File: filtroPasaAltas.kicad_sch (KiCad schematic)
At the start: 7 parts, among them U2 TL082

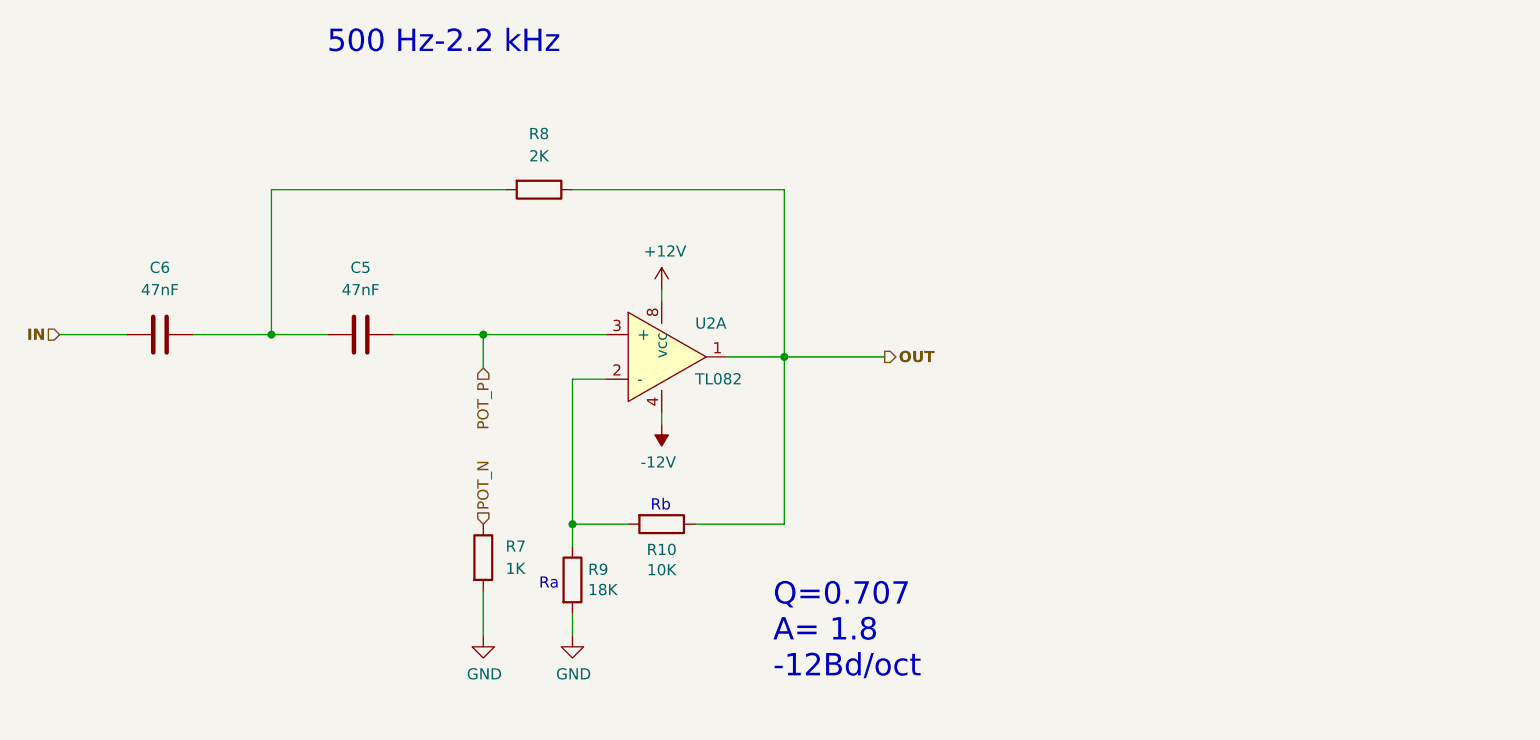
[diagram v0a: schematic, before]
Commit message: agregando control de volumen de medios, corrigiendo espacio de potenciometro doble
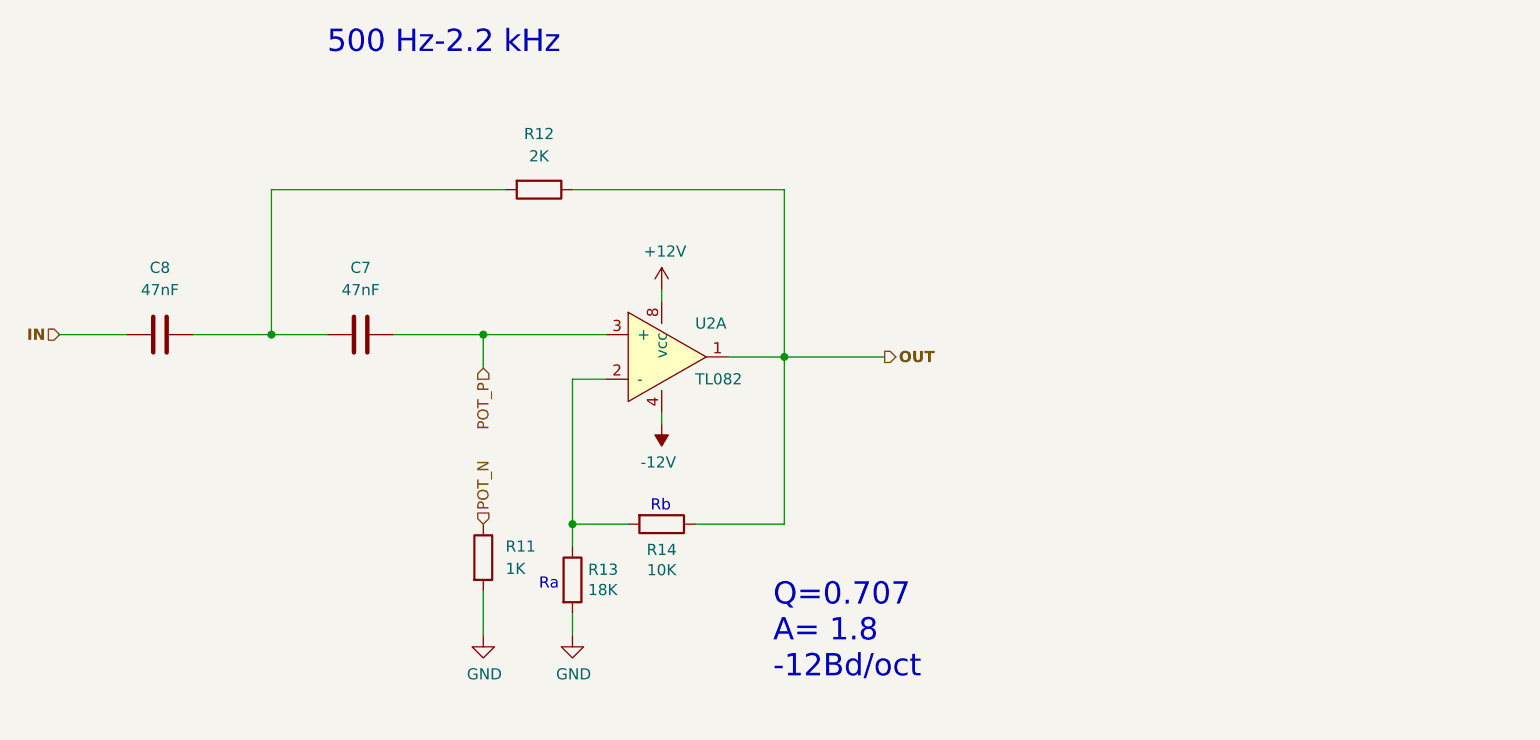
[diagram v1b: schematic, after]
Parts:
- renumbered C5 to C7, C6 to C8, R7 to R11, R8 to R12, R9 to R13, R10 to R14
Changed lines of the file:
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@@
   (symbol (lib_id "Device:R") (at 86.36 88.9 0)
     (in_bom yes) (on_board yes) (fields_autoplaced)
-    (property "Reference" "R7" (id 0) (at 88.9 87.6299 0)
+    (property "Reference" "R11" (id 0) (at 88.9 87.6299 0)
       (effects (font (size 1.27 1.27)) (justify left))
     )
@@
   (symbol (lib_id "Device:R") (at 92.71 46.99 270)
     (in_bom yes) (on_board yes) (fields_autoplaced)
-    (property "Reference" "R8" (id 0) (at 92.71 40.64 90))
+    (property "Reference" "R12" (id 0) (at 92.71 40.64 90))
     (property "Value" "2K" (id 1) (at 92.71 43.18 90))
     (property "Footprint" "Resistor_THT:R_Axial_DIN0207_L6.3mm_D2.5mm_P10.16mm_Horizontal" (id 2) (at 92.71 45.212 90)
@@
   (symbol (lib_id "Device:R") (at 96.52 91.44 0)
     (in_bom yes) (on_board yes)
-    (property "Reference" "R9" (id 0) (at 98.298 90.2716 0)
+    (property "Reference" "R13" (id 0) (at 98.298 90.2716 0)
       (effects (font (size 1.27 1.27)) (justify left))
     )
@@
   (symbol (lib_id "Device:R") (at 106.68 85.09 270)
     (in_bom yes) (on_board yes)
-    (property "Reference" "R10" (id 0) (at 106.68 88.011 90))
+    (property "Reference" "R14" (id 0) (at 106.68 88.011 90))
     (property "Value" "10K" (id 1) (at 106.68 90.3224 90))
     (property "Footprint" "Resistor_THT:R_Axial_DIN0207_L6.3mm_D2.5mm_P10.16mm_Horizontal" (id 2) (at 106.68 83.312 90)
@@
   (symbol (lib_id "Device:C") (at 49.53 63.5 270)
     (in_bom yes) (on_board yes) (fields_autoplaced)
-    (property "Reference" "C6" (id 0) (at 49.53 55.88 90))
+    (property "Reference" "C8" (id 0) (at 49.53 55.88 90))
     (property "Value" "47nF" (id 1) (at 49.53 58.42 90))
     (property "Footprint" "Capacitor_THT:C_Disc_D4.3mm_W1.9mm_P5.00mm" (id 2) (at 45.72 64.4652 0)
@@
   (symbol (lib_id "Device:C") (at 72.39 63.5 270)
     (in_bom yes) (on_board yes) (fields_autoplaced)
-    (property "Reference" "C5" (id 0) (at 72.39 55.88 90))
+    (property "Reference" "C7" (id 0) (at 72.39 55.88 90))
     (property "Value" "47nF" (id 1) (at 72.39 58.42 90))
     (property "Footprint" "Capacitor_THT:C_Disc_D4.3mm_W1.9mm_P5.00mm" (id 2) (at 68.58 64.4652 0)
@@
     (pin "4")
     (pin "8")
-    (pin "1")
-    (pin "2")
-    (pin "3")
+    (pin "5")
+    (pin "6")
+    (pin "7")
   )
 )

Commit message: agregando archivos pdf
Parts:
- renumbered C7 to C5, C8 to C6, R14 to R10, R11 to R7, R12 to R8, R13 to R9
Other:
- company: (none) -> Maykol Rey
- title: (none) -> Crossover
- moved on the sheet: C5, C6, R10, R7, R8, R9, U2A
